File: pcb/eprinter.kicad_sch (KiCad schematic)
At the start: 34 parts, among them J1 Conn_01x02_Pin, J2 Conn_01x08_Pin, J3 USB_C_Receptacle_USB2.0_14P, U1 MIC841HYC5, U2 XC6220B331MR, U3 ESP32-C3-WROOM-02

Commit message: PCB design work
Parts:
- removed J3: USB_C_Receptacle_USB2.0_14P, Capacitor_SMD:C_0603_1608Metric, symbol Connector:USB_C_Receptacle_USB2.0_14P
- added J3: USB_C_Receptacle_USB2.0_16P, eprinter:USB-C_SMD-TYPE-C-31-M-12_1, symbol eprinter:USB_C_Receptacle_USB2.0_16P
- added R1: 1, Resistor_SMD:R_0603_1608Metric, symbol Device:R
- added R8: 0.1, Resistor_SMD:R_0603_1608Metric, symbol Device:R
- added TP1, TP2, TP3, TP4: TestPoint, TestPoint:TestPoint_Pad_1.0x1.0mm, symbol Connector:TestPoint
- J1: footprint Connector_Wire:SolderWire-0.5sqmm_1x02_P4.6mm_D0.9mm_OD2.1mm -> Connector_PinHeader_2.54mm:PinHeader_1x02_P2.54mm_Vertical
- J2: footprint Connector_PinHeader_2.54mm:PinHeader_2x04_P2.54mm_Vertical -> Connector_PinHeader_2.54mm:PinHeader_1x08_P2.54mm_Vertical
- TP5: renamed from TP1; footprint (none) -> TestPoint:TestPoint_Pad_1.0x1.0mm
- TP6: renamed from TP2; footprint (none) -> TestPoint:TestPoint_Pad_1.0x1.0mm
- renumbered D4 to D3, D3 to D4, R8 to R10, R9 to R11, R10 to R12, R11 to R13, R12 to R14, R13 to R15, R14 to R16, R15 to R17, R1 to R4, R4 to R5, R5 to R6, R6 to R7, R7 to R9
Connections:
- net GND: now also J3.1 (SHIELD), J3.2 (SHIELD), J3.3 (SHIELD), J3.4 (SHIELD), J3.A1B12 (GND), J3.B1A12 (GND)
- net SOLAR+: now also R1.1, TP1.1; no longer D1.2 (A)
- net USB_5V: now also J3.A4B9 (VBUS), J3.B4A9 (VBUS)
- net VIN: now also R8.2, TP4.1; no longer C1.1, D1.1 (K), D2.1 (K), D4.1 (K)
- net at R3.2: now also J3.A6 (D+), J3.B6 (D+)
- net at R5.1: now also J3.B5 (CC2)
- net at R7.1: now also J3.A5 (CC1)
- net at R2.1: now also J3.A7 (D-), J3.B7 (D-)
- new net: D1.2 (A), R1.2, TP2.1
- new net: C1.1, D1.1 (K), D2.1 (K), D4.1 (K), R8.1, TP3.1
- no-connect marks 3 -> 5
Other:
- moved on the sheet: C1, D1, D2, D4, R4

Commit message: Refactor PCB
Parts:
- removed D1: PMEG2010AEJ, Diode_SMD:D_SOD-323F, symbol Diode:PMEG2010AEJ
- removed D4: 1N4733A, Diode_THT:D_DO-41_SOD81_P10.16mm_Horizontal, symbol Diode:1N47xxA
- removed R4: 22, Resistor_SMD:R_2512_6332Metric, symbol Device:R
- added D1: BAT54J, Diode_SMD:D_SOD-323F, symbol Diode:BAT54J
- added R2, R3, R6: 10k, Resistor_SMD:R_0603_1608Metric, symbol Device:R
- added U1: TL431DBZ, Package_TO_SOT_SMD:SOT-23, symbol Reference_Voltage:TL431DBZ
- added U5: LM66100DCK, Package_TO_SOT_SMD:SOT-363_SC-70-6, symbol Power_Management:LM66100DCK
- renumbered R8 to R10, R9 to R11, R10 to R12, R11 to R13, R12 to R14, R13 to R15, R14 to R16, R15 to R17, R16 to R18, R17 to R19, R2 to R4, R3 to R5, R5 to R7, R6 to R8, R7 to R9, U1 to U2, U2 to U3, U3 to U4
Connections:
- net GND: now also R3.2, R6.2, U1.3 (A), U5.2 (GND), U5.5 (ST)
- net USB_5V: now also D2.2 (A), R6.1, U5.3 (~{CE})
- net at R1.2, TP2.1: now also D1.2 (A), R2.1, U1.1 (K)
- net at D2.1 (K), R10.1, TP3.1: now also U5.6 (VOUT); no longer C1.1
- new net: C1.1, D1.1 (K), U5.1 (VIN)
- new net: R2.2, R3.1, U1.2 (REF)
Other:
- moved on the sheet: C1, C2, C3, C5, C6, D3, J1, J2, J3, R1, R10, R11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

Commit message: Finalize silk screen
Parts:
- removed TP1, TP2, TP3, TP4: TestPoint, TestPoint:TestPoint_Pad_1.0x1.0mm, symbol Connector:TestPoint
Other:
- moved on the sheet: C2, C3, C4, C7, D3, J1, J2, J3, R10, R11, R12, R13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

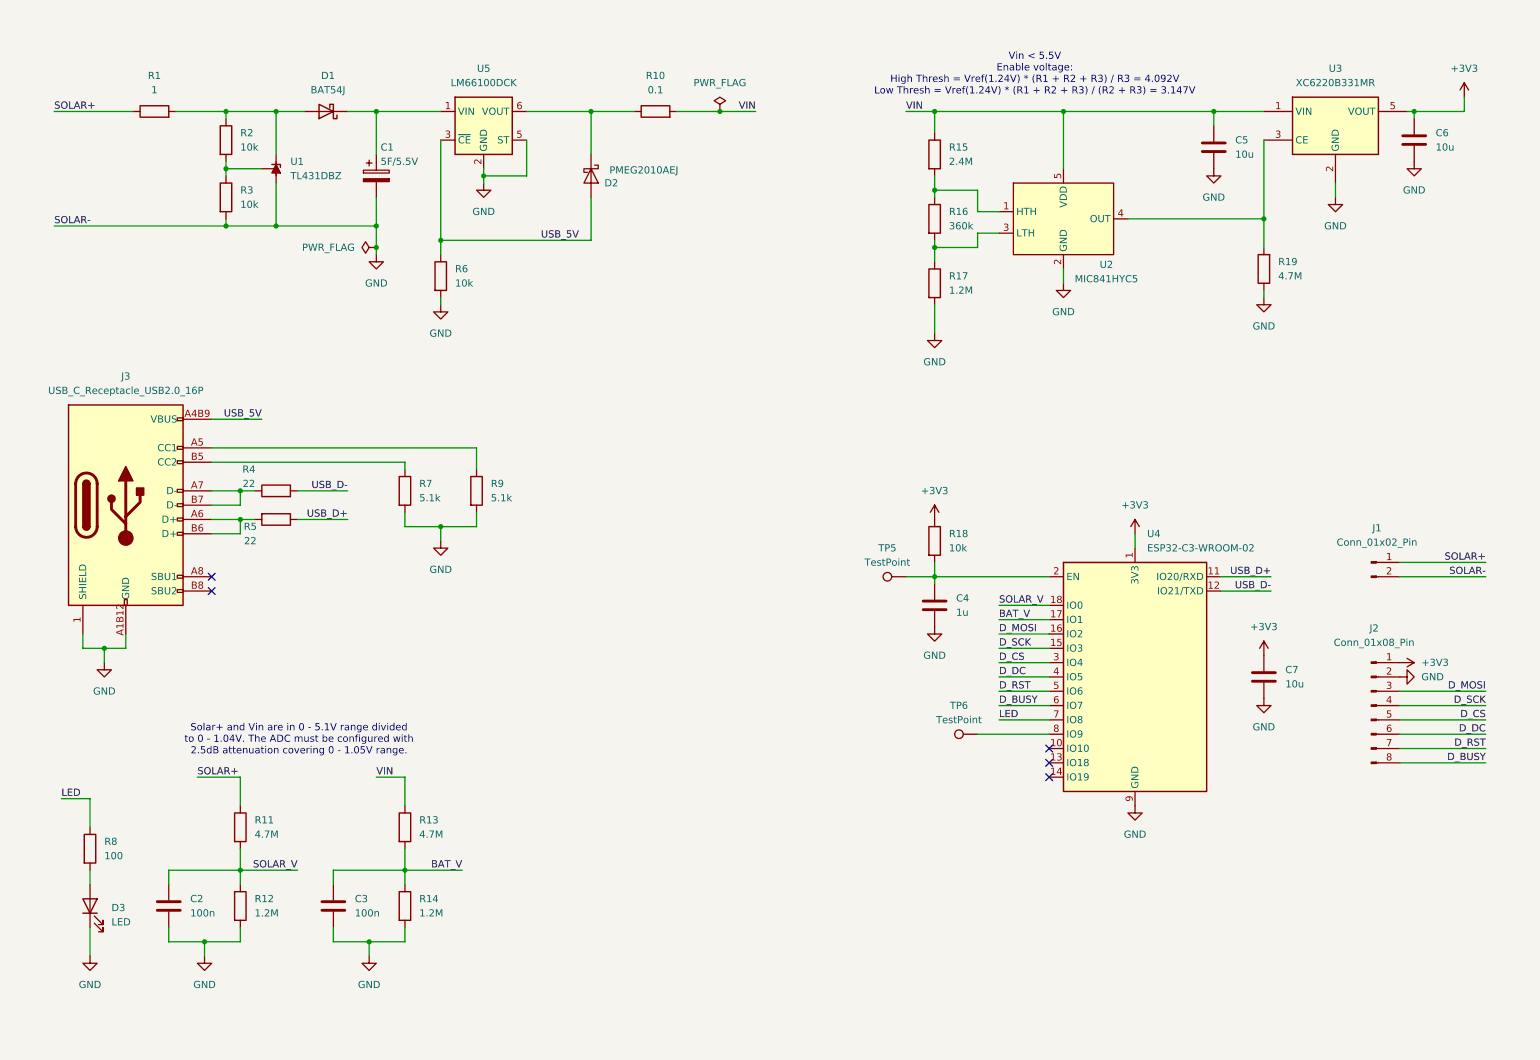
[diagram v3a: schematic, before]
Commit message: Display driver schematic
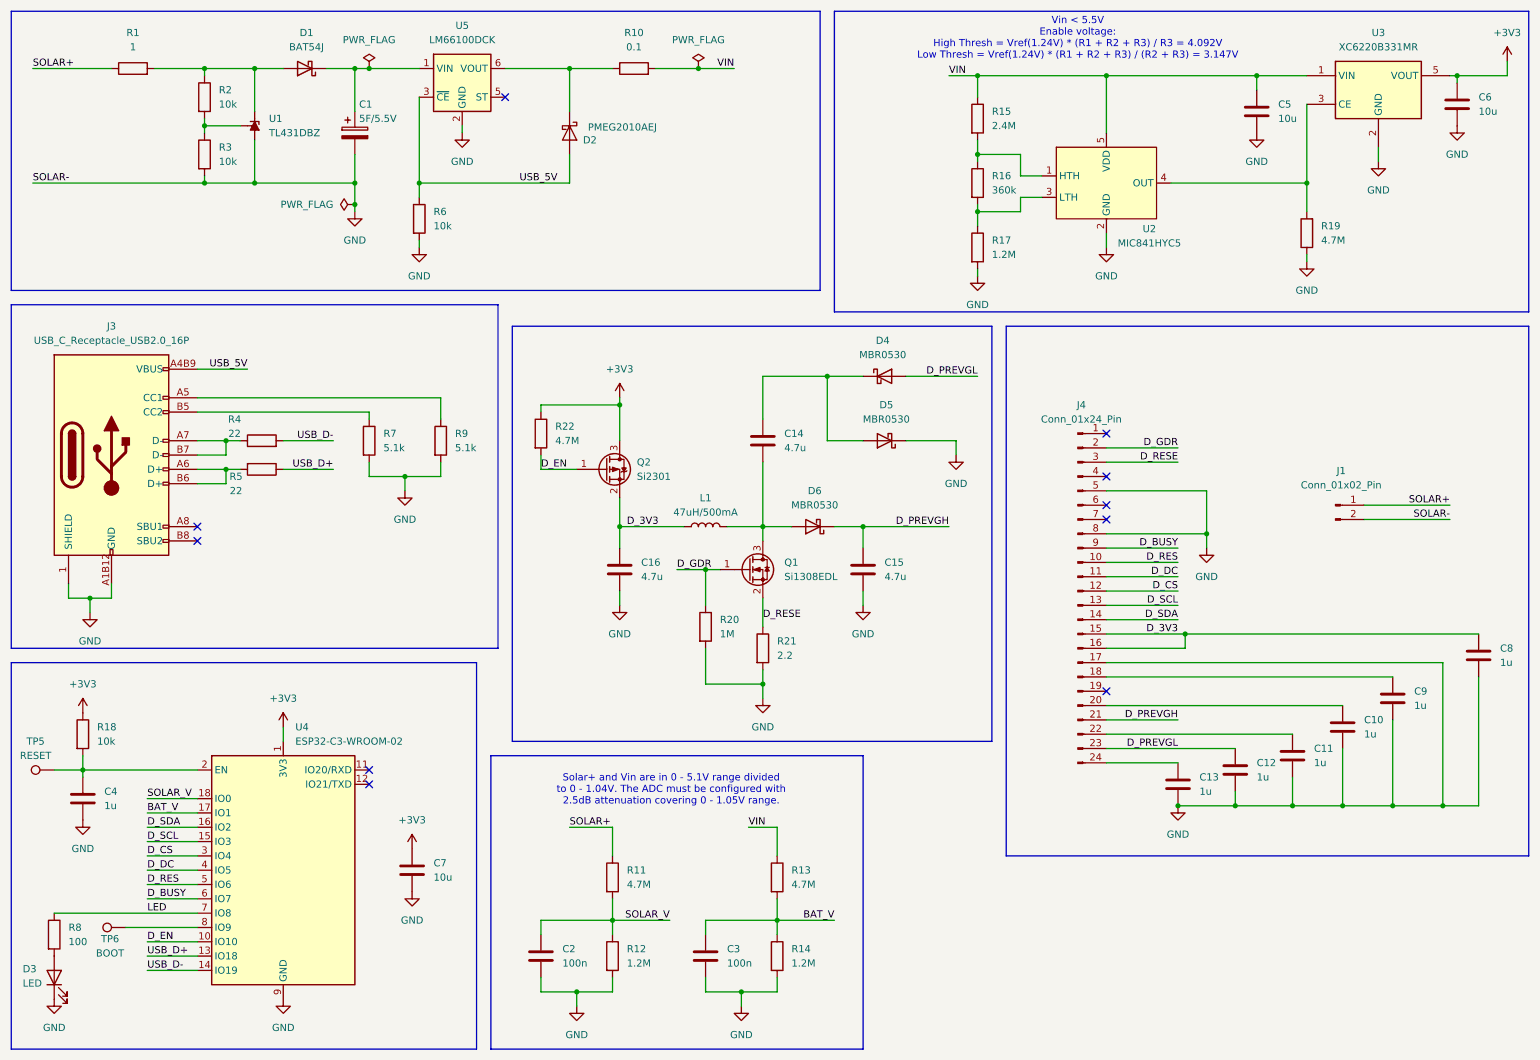
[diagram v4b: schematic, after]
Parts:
- removed J2: Conn_01x08_Pin, Connector_PinHeader_2.54mm:PinHeader_1x08_P2.54mm_Vertical, symbol Connector:Conn_01x08_Pin
- added C10, C11, C12, C13, C8, C9: 1u, symbol Device:C
- added C14, C15, C16: 4.7u, Diode_SMD:D_SOD-123, symbol Device:C
- added D4, D5, D6: MBR0530, Diode_SMD:D_SOD-123, symbol Diode:MBR0530
- added J4: Conn_01x24_Pin, Package_SO:SOIC-8_3.9x4.9mm_P1.27mm, symbol Connector:Conn_01x24_Pin
- added L1: 47uH/500mA, symbol Device:L
- added Q1: Si1308EDL, Package_TO_SOT_SMD:SOT-323_SC-70, symbol Transistor_FET:Si1308EDL
- added Q2: Si2301, Package_TO_SOT_SMD:SOT-23, symbol eprinter:Si2301
- added R20: 1M, Package_TO_SOT_SMD:SOT-323_SC-70, symbol Device:R
- added R21: 2.2, Package_TO_SOT_SMD:SOT-323_SC-70, symbol Device:R
- added R22: 4.7M, Resistor_SMD:R_0603_1608Metric, symbol Device:R
- TP5: value TestPoint -> RESET
- TP6: value TestPoint -> BOOT
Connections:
- net +3V3: now also Q2.3 (D), R22.1
- net D_BUSY: now also J4.9 (Pin_9)
- net D_CS: now also J4.12 (Pin_12)
- net D_DC: now also J4.11 (Pin_11)
- net GND: now also C10.2, C11.2, C12.2, C13.2, C15.2, C16.2, C8.2, C9.2, D5.1 (K), J4.17 (Pin_17), J4.5 (Pin_5), J4.8 (Pin_8), R20.2, R21.2; no longer U5.5 (ST)
- net USB_D+: now also U4.13 (IO18); no longer U4.11 (IO20/RXD)
- net USB_D-: now also U4.14 (IO19); no longer U4.12 (IO21/TXD)
- net D_EN: now reaches U4.10 (IO10)
- net D_EN: now also Q2.1 (G), R22.2
- net D_MOSI renamed D_SDA
- net D_SDA: now also J4.14 (Pin_14)
- net D_RST renamed D_RES
- net D_RES: now also J4.10 (Pin_10)
- net D_SCK renamed D_SCL
- net D_SCL: now also J4.13 (Pin_13)
- new net: C10.1, J4.20 (Pin_20)
- new net: C14.2, D6.2 (A), L1.2, Q1.3 (D)
- new net: C13.1, J4.24 (Pin_24)
- new net: C14.1, D4.1 (K), D5.2 (A)
- new net: C11.1, J4.22 (Pin_22)
- new net: C9.1, J4.18 (Pin_18)
- new net D_3V3: C16.1, C8.1, J4.15 (Pin_15), J4.16 (Pin_16), L1.1, Q2.2 (S)
- new net D_GDR: J4.2 (Pin_2), Q1.1 (G), R20.1
- new net D_PREVGH: C15.1, D6.1 (K), J4.21 (Pin_21)
- new net D_PREVGL: C12.1, D4.2 (A), J4.23 (Pin_23)
- new net D_RESE: J4.3 (Pin_3), Q1.2 (S), R21.1
- no-connect marks 5 -> 10
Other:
- moved on the sheet: C1, C2, C3, C4, C5, C6, C7, D1, D2, D3, J1, J3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

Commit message: Schematic verification
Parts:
- removed C4: 1u, Capacitor_SMD:C_0603_1608Metric, symbol Device:C
- removed D2: PMEG2010AEJ, Diode_SMD:D_SOD-323F, symbol Diode:PMEG2010AEJ
- removed D3: LED, LED_SMD:LED_0603_1608Metric, symbol Device:LED
- removed J4: Conn_01x24_Pin, Package_SO:SOIC-8_3.9x4.9mm_P1.27mm, symbol Connector:Conn_01x24_Pin
- removed R18: 10k, Resistor_SMD:R_0603_1608Metric, symbol Device:R
- removed TP5: RESET, TestPoint:TestPoint_Pad_1.0x1.0mm, symbol Connector:TestPoint
- removed TP6: BOOT, TestPoint:TestPoint_Pad_1.0x1.0mm, symbol Connector:TestPoint
- added C12, C3: 1u, Capacitor_SMD:C_0603_1608Metric, symbol Device:C
- added D2: LED, LED_SMD:LED_0603_1608Metric, symbol Device:LED
- added D3: PMEG2010AEJ, Diode_SMD:D_SOD-323F, symbol Diode:PMEG2010AEJ
- added J2: Conn_01x26_Pin, eprinter:FPC-SMD_AFC07-S24FCC-00, symbol Connector:Conn_01x26_Pin
- added R9: 10k, Resistor_SMD:R_0603_1608Metric, symbol Device:R
- added SW1, SW2: SW_Push, eprinter:SW-SMD_L3.9-W3.0-P4.45, symbol Switch:SW_Push
- C11: renamed from C12; footprint (none) -> Capacitor_SMD:C_0603_1608Metric
- C13: renamed from C11; footprint (none) -> Capacitor_SMD:C_0603_1608Metric
- C14: renamed from C10; footprint (none) -> Capacitor_SMD:C_0603_1608Metric
- C15: renamed from C9; footprint (none) -> Capacitor_SMD:C_0603_1608Metric
- C17: renamed from C8; footprint (none) -> Capacitor_SMD:C_0603_1608Metric
- C5: renamed from C16; footprint Diode_SMD:D_SOD-123 -> Capacitor_SMD:C_0603_1608Metric
- C7: renamed from C14; footprint Diode_SMD:D_SOD-123 -> Capacitor_SMD:C_0603_1608Metric
- C8: renamed from C15; footprint Diode_SMD:D_SOD-123 -> Capacitor_SMD:C_0603_1608Metric
- C9: renamed from C13; footprint (none) -> Capacitor_SMD:C_0603_1608Metric
- L1: footprint (none) -> eprinter:IND-SMD_L3.0-W3.0-1
- R11: renamed from R22; value 4.7M -> 10k
- R15: renamed from R20; footprint Package_TO_SOT_SMD:SOT-323_SC-70 -> Resistor_SMD:R_0603_1608Metric
- R16: renamed from R21; footprint Package_TO_SOT_SMD:SOT-323_SC-70 -> Resistor_SMD:R_0603_1608Metric
- renumbered C5 to C10, C6 to C16, C7 to C2, C2 to C4, C3 to C6, D6 to D4, D4 to D5, D5 to D6, J3 to J1, J1 to J3, Q2 to Q1, Q1 to Q2, R9 to R10, R10 to R12, R11 to R13, R12 to R14, R13 to R17, R14 to R18, R15 to R19, R16 to R20, R17 to R21, R19 to R22, U4 to U1, U1 to U2, U5 to U3, U2 to U4, U3 to U5
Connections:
- net +3V3: now also R6.1, R9.1
- net D_3V3: now also J2.15 (Pin_15), J2.16 (Pin_16)
- net D_BUSY: now also J2.9 (Pin_9)
- net D_CS: now also J2.12 (Pin_12)
- net D_DC: now also J2.11 (Pin_11)
- net D_GDR: now also J2.2 (Pin_2)
- net D_PREVGH: now also J2.21 (Pin_21)
- net D_PREVGL: now also J2.23 (Pin_23)
- net D_RES: now also J2.10 (Pin_10)
- net D_RESE: now also J2.3 (Pin_3)
- net D_SCL: now also J2.13 (Pin_13)
- net D_SDA: now also J2.14 (Pin_14)
- net GND: now also C12.2, C3.2, D2.1 (K), J2.17 (Pin_17), J2.25 (Pin_25), J2.26 (Pin_26), J2.8 (Pin_8), SW1.1, SW2.1; no longer R6.2
- net USB_5V: now also D3.2 (A); no longer R6.1, U3.3 (~{CE})
- net USB_D+: now also U1.14 (IO19); no longer U1.13 (IO18)
- net USB_D-: now also U1.13 (IO18); no longer U1.14 (IO19)
- net at R12.1, U3.6 (VOUT): now also U3.3 (~{CE}), D3.1 (K)
- net D_VSH1: now reaches C14.1
- net D_VSH1: now also J2.20 (Pin_20)
- net CHIP_EN: now reaches U1.2 (EN)
- net CHIP_EN: now also R6.2, C3.1, SW1.2
- net at R8.2: now also D2.2 (A)
- net D_VCOM: now reaches C9.1
- net D_VCOM: now also J2.24 (Pin_24)
- net D_VSL: now reaches C13.1
- net D_VSL: now also J2.22 (Pin_22)
- net BOOT: now reaches U1.8 (IO9)
- net BOOT: now also R9.2, SW2.2
- net D_VDD: now reaches C15.1
- net D_VDD: now also J2.18 (Pin_18)
- new net D_TSCL: J2.6 (Pin_6)
- new net D_TSDA: J2.7 (Pin_7)
- new net D_VPP: J2.19 (Pin_19)
- new net D_VSH2: C12.1, J2.5 (Pin_5)
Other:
- note added: "LM66100 functions in reverse current blocking (RCB) mode"
- moved on the sheet: C1, C11, C13, C14, C15, C17, C2, C4, C5, C6, C7, C8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

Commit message: Routing done
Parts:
- removed D3: PMEG2010AEJ, Diode_SMD:D_SOD-323F, symbol Diode:PMEG2010AEJ
- removed U2: TL431DBZ, Package_TO_SOT_SMD:SOT-23, symbol Reference_Voltage:TL431DBZ
- added D3: PMEG2010EJ, Diode_SMD:D_SOD-323F, symbol Diode:PMEG2010EJ
- added U2: LM431BIM3X, Package_TO_SOT_SMD:SOT-23, symbol eprinter:LM431BIM3X
- C1, J3: now left out of the parts list
- D1: LCSC (none) -> C130415
- D4, D5, D6: LCSC (none) -> C82046
- J1: LCSC (none) -> C165948
- J2: value Conn_01x26_Pin -> AFC07-S24FCC-00; LCSC (none) -> C720477
- L1: LCSC (none) -> C76865
- Q1: LCSC (none) -> C10487
- Q2: LCSC (none) -> C469327
- SW1: value SW_Push -> RESET; LCSC (none) -> C720477
- SW2: value SW_Push -> BOOT; LCSC (none) -> C720477
- U1: LCSC (none) -> C2934560
- U3: LCSC (none) -> C2869734
- U4: LCSC (none) -> C511290
- U5: LCSC (none) -> C86534
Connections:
- net GND: now also U2.3 (A)
- net USB_5V: now also D3.2 (A)
- net at R12.1, U3.3 (~{CE}), U3.6 (VOUT): now also D3.1 (K)
- net at D1.2 (A), R1.2, R2.1: now also U2.1 (K)
- net at R2.2, R3.1: now also U2.2 (REF)
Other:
- note added: "Taken from GDEY042Z98 (4.2") datasheet TODO: see what components need to be changed for different sizes"

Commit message: PCB silkscreen done and LCSC part selection
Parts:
- C1, J3: now not fitted
- C10, C16, C2: LCSC (none) -> C77040
- C11, C12, C13, C14, C15, C17, C3, C9: LCSC (none) -> C77046
- C4, C6: LCSC (none) -> C77050
- C5, C7, C8: LCSC (none) -> C90057
- D2: LCSC (none) -> C83242
- R1: LCSC (none) -> C2077177
- R10, R7: LCSC (none) -> C844375
- R11, R2, R3, R6, R9: LCSC (none) -> C169103
- R12: LCSC (none) -> C844273
- R13, R17, R22: LCSC (none) -> C123423
- R14, R18, R21: LCSC (none) -> C844338
- R15: LCSC (none) -> C313691
- R16: LCSC (none) -> C2086340
- R19: LCSC (none) -> C3008968
- R20: LCSC (none) -> C844159
- R4, R5: LCSC (none) -> C71618
- R8: LCSC (none) -> C844724
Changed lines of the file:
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@@
 			)
 		)
-		(property "LCSC" ""
+		(property "LCSC" "C77040"
 			(at 234.95 30.48 0)
 			(hide yes)
@@
 			)
 		)
-		(property "LCSC" ""
+		(property "LCSC" "C123423"
 			(at 243.84 52.07 0)
 			(hide yes)
@@
 			)
 		)
-		(property "LCSC" ""
+		(property "LCSC" "C2077177"
 			(at 35.56 29.21 90)
 			(hide yes)
@@
 			)
 		)
-		(property "LCSC" ""
+		(property "LCSC" "C77046"
 			(at 254 134.62 0)
 			(hide yes)
@@
 			)
 		)
-		(property "LCSC" ""
+		(property "LCSC" "C169103"
 			(at 115.57 87.63 0)
 			(hide yes)
@@
 			)
 		)
-		(property "LCSC" ""
+		(property "LCSC" "C77050"
 			(at 148.59 180.34 0)
 			(hide yes)
@@
 			)
 		)
-		(property "LCSC" ""
+		(property "LCSC" "C169103"
 			(at 77.47 166.37 0)
 			(hide yes)
@@
 			)
 		)
-		(property "LCSC" ""
+		(property "LCSC" "C77040"
 			(at 270.51 29.21 0)
 			(hide yes)
@@
 			)
 		)
-		(property "LCSC" ""
+		(property "LCSC" "C77040"
 			(at 77.47 140.97 0)
 			(hide yes)
@@
 			)
 		)
-		(property "LCSC" ""
+		(property "LCSC" "C71618"
 			(at 63.5 92.71 90)
 			(hide yes)
@@
 			)
 		)
-		(property "LCSC" ""
+		(property "LCSC" "C844159"
 			(at 185.42 43.18 0)
 			(hide yes)
@@
 			)
 		)
-		(property "LCSC" ""
+		(property "LCSC" "C3008968"
 			(at 185.42 31.75 0)
 			(hide yes)
@@
 		(in_bom no)
 		(on_board yes)
-		(in_pos_files yes)
-		(dnp no)
+		(in_pos_files no)
+		(dnp yes)
 		(property "Reference" "J3"
 			(at 253.746 89.154 0)
@@
 			)
 		)
-		(property "LCSC" ""
+		(property "LCSC" "C90057"
 			(at 172.72 111.76 0)
 			(hide yes)
@@
 			)
 		)
-		(property "LCSC" ""
+		(property "LCSC" "C844375"
 			(at 82.55 87.63 0)
 			(hide yes)
@@
 			)
 		)
-		(property "LCSC" ""
+		(property "LCSC" "C83242"
 			(at 93.98 143.51 90)
 			(hide yes)
@@
 			)
 		)
-		(property "LCSC" ""
+		(property "LCSC" "C844338"
 			(at 185.42 54.61 0)
 			(hide yes)
@@
 			)
 		)
-		(property "LCSC" ""
+		(property "LCSC" "C77046"
 			(at 237.49 97.79 0)
 			(hide yes)
@@
 			)
 		)
-		(property "LCSC" ""
+		(property "LCSC" "C77046"
 			(at 224.79 144.78 0)
 			(hide yes)
@@
 			)
 		)
-		(property "LCSC" ""
+		(property "LCSC" "C169103"
 			(at 48.26 34.29 0)
 			(hide yes)
@@
 			)
 		)
-		(property "LCSC" ""
+		(property "LCSC" "C123423"
 			(at 132.08 166.37 0)
 			(hide yes)
@@
 			)
 		)
-		(property "LCSC" ""
+		(property "LCSC" "C71618"
 			(at 63.5 87.63 90)
 			(hide yes)
@@
 			)
 		)
-		(property "LCSC" ""
+		(property "LCSC" "C77046"
 			(at 245.11 139.7 0)
 			(hide yes)
@@
 			)
 		)
-		(property "LCSC" ""
+		(property "LCSC" "C313691"
 			(at 144.78 121.92 0)
 			(hide yes)
@@
 			)
 		)
-		(property "LCSC" ""
+		(property "LCSC" "C77046"
 			(at 234.95 142.24 0)
 			(hide yes)
@@
 			)
 		)
-		(property "LCSC" ""
+		(property "LCSC" "C77050"
 			(at 119.38 180.34 0)
 			(hide yes)
@@
 			)
 		)
-		(property "LCSC" ""
+		(property "LCSC" "C90057"
 			(at 129.54 111.76 0)
 			(hide yes)
@@
 		(in_bom no)
 		(on_board yes)
-		(in_pos_files yes)
-		(dnp no)
+		(in_pos_files no)
+		(dnp yes)
 		(property "Reference" "C1"
 			(at 75.692 35.56 0)
@@
 			)
 		)
-		(property "LCSC" ""
+		(property "LCSC" "C844724"
 			(at 93.98 135.89 0)
 			(hide yes)
@@
 			)
 		)
-		(property "LCSC" ""
+		(property "LCSC" "C169103"
 			(at 48.26 44.45 0)
 			(hide yes)
@@
 			)
 		)
-		(property "LCSC" ""
+		(property "LCSC" "C169103"
 			(at 93.98 166.37 0)
 			(hide yes)
@@
 			)
 		)
-		(property "LCSC" ""
+		(property "LCSC" "C123423"
 			(at 161.29 166.37 0)
 			(hide yes)
@@
 			)
 		)
-		(property "LCSC" ""
+		(property "LCSC" "C844375"
 			(at 95.25 87.63 0)
 			(hide yes)
@@
 			)
 		)
-		(property "LCSC" ""
+		(property "LCSC" "C77046"
 			(at 274.32 121.92 0)
 			(hide yes)
@@
 			)
 		)
-		(property "LCSC" ""
+		(property "LCSC" "C77046"
 			(at 262.89 129.54 0)
 			(hide yes)
@@
 			)
 		)
-		(property "LCSC" ""
+		(property "LCSC" "C844338"
 			(at 161.29 180.34 0)
 			(hide yes)
@@
 			)
 		)
-		(property "LCSC" ""
+		(property "LCSC" "C90057"
 			(at 154.94 88.9 0)
 			(hide yes)
@@
 			)
 		)
-		(property "LCSC" ""
+		(property "LCSC" "C844273"
 			(at 124.46 29.21 90)
 			(hide yes)
@@
 			)
 		)
-		(property "LCSC" ""
+		(property "LCSC" "C2086340"
 			(at 154.94 125.73 0)
 			(hide yes)
@@
 			)
 		)
-		(property "LCSC" ""
+		(property "LCSC" "C844338"
 			(at 132.08 180.34 0)
 			(hide yes)
@@
 			)
 		)
-		(property "LCSC" ""
+		(property "LCSC" "C77046"
 			(at 77.47 179.07 0)
 			(hide yes)
